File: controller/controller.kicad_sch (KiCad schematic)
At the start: 2 parts, among them U1 XIAO-RP2040-DIP

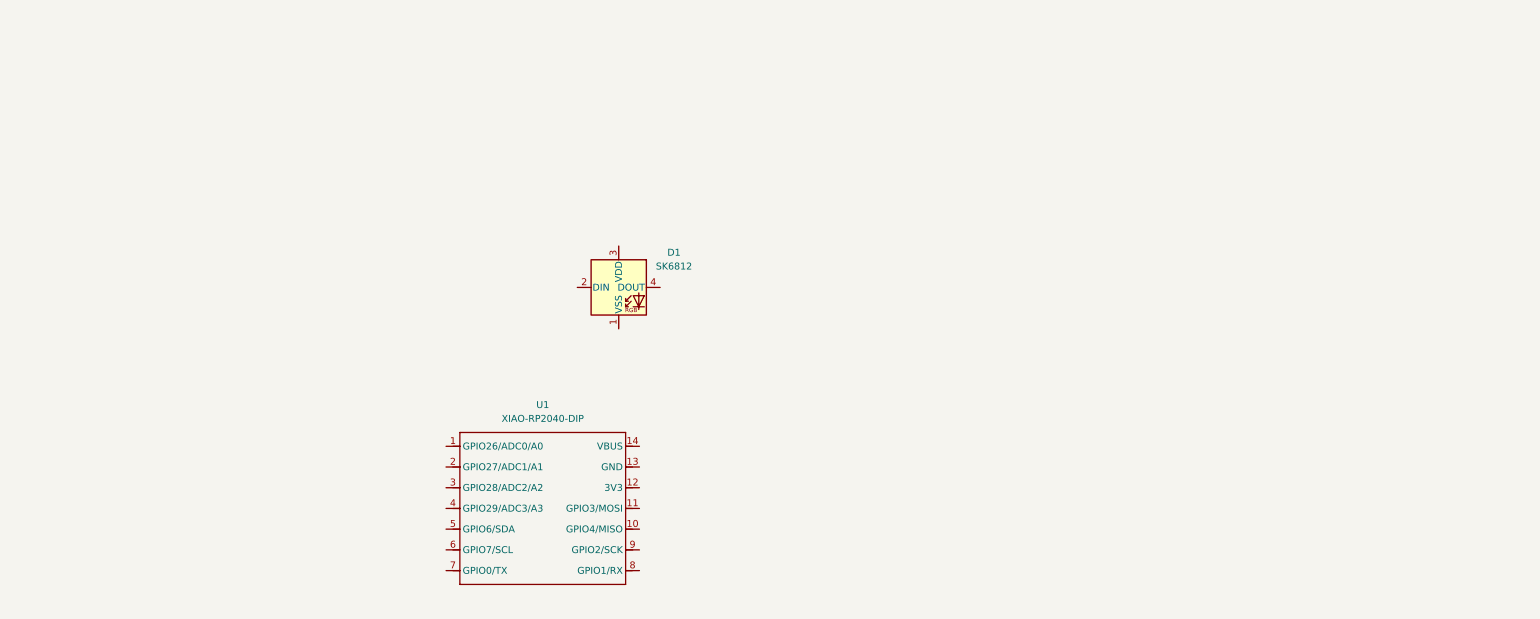
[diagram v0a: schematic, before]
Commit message: New controller design
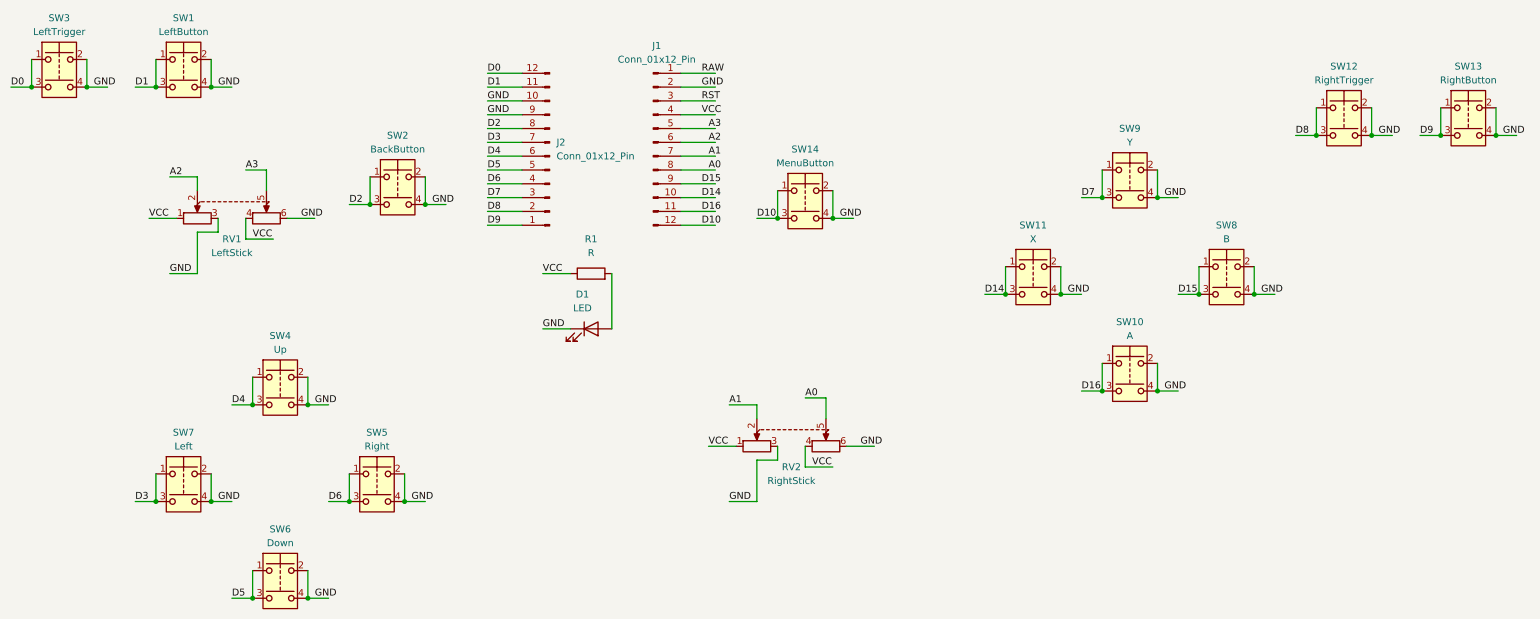
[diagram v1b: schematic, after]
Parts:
- removed D1: SK6812, LED_SMD:LED_SK6812_PLCC4_5.0x5.0mm_P3.2mm, symbol LED:SK6812
- removed U1: XIAO-RP2040-DIP, Module:MOUDLE14P-XIAO-DIP-SMD, symbol OPL Library:XIAO-RP2040-DIP
- added D1: LED, LED_THT:LED_D5.0mm, symbol Device:LED
- added J1, J2: Conn_01x12_Pin, Connector_PinHeader_2.54mm:PinHeader_1x12_P2.54mm_Vertical, symbol Connector:Conn_01x12_Pin
- added R1: R, Resistor_THT:R_Axial_DIN0207_L6.3mm_D2.5mm_P10.16mm_Horizontal, symbol Device:R
- added RV1: LeftStick, MEGA Downloads:JOYSTICK, symbol Device:R_Potentiometer_Dual
- added RV2: RightStick, MEGA Downloads:JOYSTICK, symbol Device:R_Potentiometer_Dual
- added SW1: LeftButton, Button_Switch_THT:SW_Tactile_SKHH_Angled, symbol Switch:SW_Push_Dual
- added SW10: A, Button_Switch_THT:Push_E-Switch_KS01Q01, symbol Switch:SW_Push_Dual
- added SW11: X, Button_Switch_THT:Push_E-Switch_KS01Q01, symbol Switch:SW_Push_Dual
- added SW12: RightTrigger, Button_Switch_THT:SW_Tactile_SKHH_Angled, symbol Switch:SW_Push_Dual
- added SW13: RightButton, Button_Switch_THT:SW_Tactile_SKHH_Angled, symbol Switch:SW_Push_Dual
- added SW14: MenuButton, Button_Switch_THT:Push_E-Switch_KS01Q01, symbol Switch:SW_Push_Dual
- added SW2: BackButton, Button_Switch_THT:Push_E-Switch_KS01Q01, symbol Switch:SW_Push_Dual
- added SW3: LeftTrigger, Button_Switch_THT:SW_Tactile_SKHH_Angled, symbol Switch:SW_Push_Dual
- added SW4: Up, Button_Switch_THT:Push_E-Switch_KS01Q01, symbol Switch:SW_Push_Dual
- added SW5: Right, Button_Switch_THT:Push_E-Switch_KS01Q01, symbol Switch:SW_Push_Dual
- added SW6: Down, Button_Switch_THT:Push_E-Switch_KS01Q01, symbol Switch:SW_Push_Dual
- added SW7: Left, Button_Switch_THT:Push_E-Switch_KS01Q01, symbol Switch:SW_Push_Dual
- added SW8: B, Button_Switch_THT:Push_E-Switch_KS01Q01, symbol Switch:SW_Push_Dual
- added SW9: Y, Button_Switch_THT:Push_E-Switch_KS01Q01, symbol Switch:SW_Push_Dual
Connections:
- new net: D1.2 (A), R1.2
- new net A0: J1.8 (Pin_8), RV2.5
- new net A1: J1.7 (Pin_7), RV2.2
- new net A2: J1.6 (Pin_6), RV1.2
- new net A3: J1.5 (Pin_5), RV1.5
- new net D0: J2.12 (Pin_12), SW3.1, SW3.3
- new net D1: J2.11 (Pin_11), SW1.1, SW1.3
- new net D10: J1.12 (Pin_12), SW14.1, SW14.3
- new net D14: J1.10 (Pin_10), SW11.1, SW11.3
- new net D15: J1.9 (Pin_9), SW8.1, SW8.3
- new net D16: J1.11 (Pin_11), SW10.1, SW10.3
- new net D2: J2.8 (Pin_8), SW2.1, SW2.3
- new net D3: J2.7 (Pin_7), SW7.1, SW7.3
- new net D4: J2.6 (Pin_6), SW4.1, SW4.3
- new net D5: J2.5 (Pin_5), SW6.1, SW6.3
- new net D6: J2.4 (Pin_4), SW5.1, SW5.3
- new net D7: J2.3 (Pin_3), SW9.1, SW9.3
- new net D8: J2.2 (Pin_2), SW12.1, SW12.3
- new net D9: J2.1 (Pin_1), SW13.1, SW13.3
- new net GND: D1.1 (K), J1.2 (Pin_2), J2.10 (Pin_10), J2.9 (Pin_9), RV1.3, RV1.6, RV2.3, RV2.6, SW1.2, SW1.4, SW10.2, SW10.4, SW11.2, SW11.4, SW12.2, SW12.4, SW13.2, SW13.4, SW14.2, SW14.4, SW2.2, SW2.4, SW3.2, SW3.4, SW4.2, SW4.4, SW5.2, SW5.4, SW6.2, SW6.4, SW7.2, SW7.4, SW8.2, SW8.4, SW9.2, SW9.4
- new net RAW: J1.1 (Pin_1)
- new net RST: J1.3 (Pin_3)
- new net VCC: J1.4 (Pin_4), R1.1, RV1.1, RV1.4, RV2.1, RV2.4
